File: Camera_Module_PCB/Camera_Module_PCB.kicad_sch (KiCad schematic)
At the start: 58 parts, among them J2 DM3AT-SF-PEJM5, J3 FFC2A32-24-T, J4 Conn_01x02, SW2 SW_Push, SW3 SW_Push, U2 ESP32-S3R8, U4 MAX98357AETE_T, U5 MSM261DGT003, U6 SY7200AABC, Y1 40MHz

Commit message: Minor Changes
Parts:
- renumbered U5 to Mic
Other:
- note added: "ESP 32 and Supporting Schematics"
- note added: "Microphone"
- note added: "Optical Sensor"
- note removed: "Are pull-up resistors needed because I2C communication requires idle high?"
- note removed: "Honestly idk why the resistors are used here. If u know please lmk why."
- note removed: "Made all conections to the MCU, but there is still the issue of power. I cannot find alternative regulators for 2.8 & 1.5. I'm sure I can find some soon tho"
- moved on the sheet: C, C1, C11, C12, C13, C14, C15, C16, C2, C24, C25, C26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

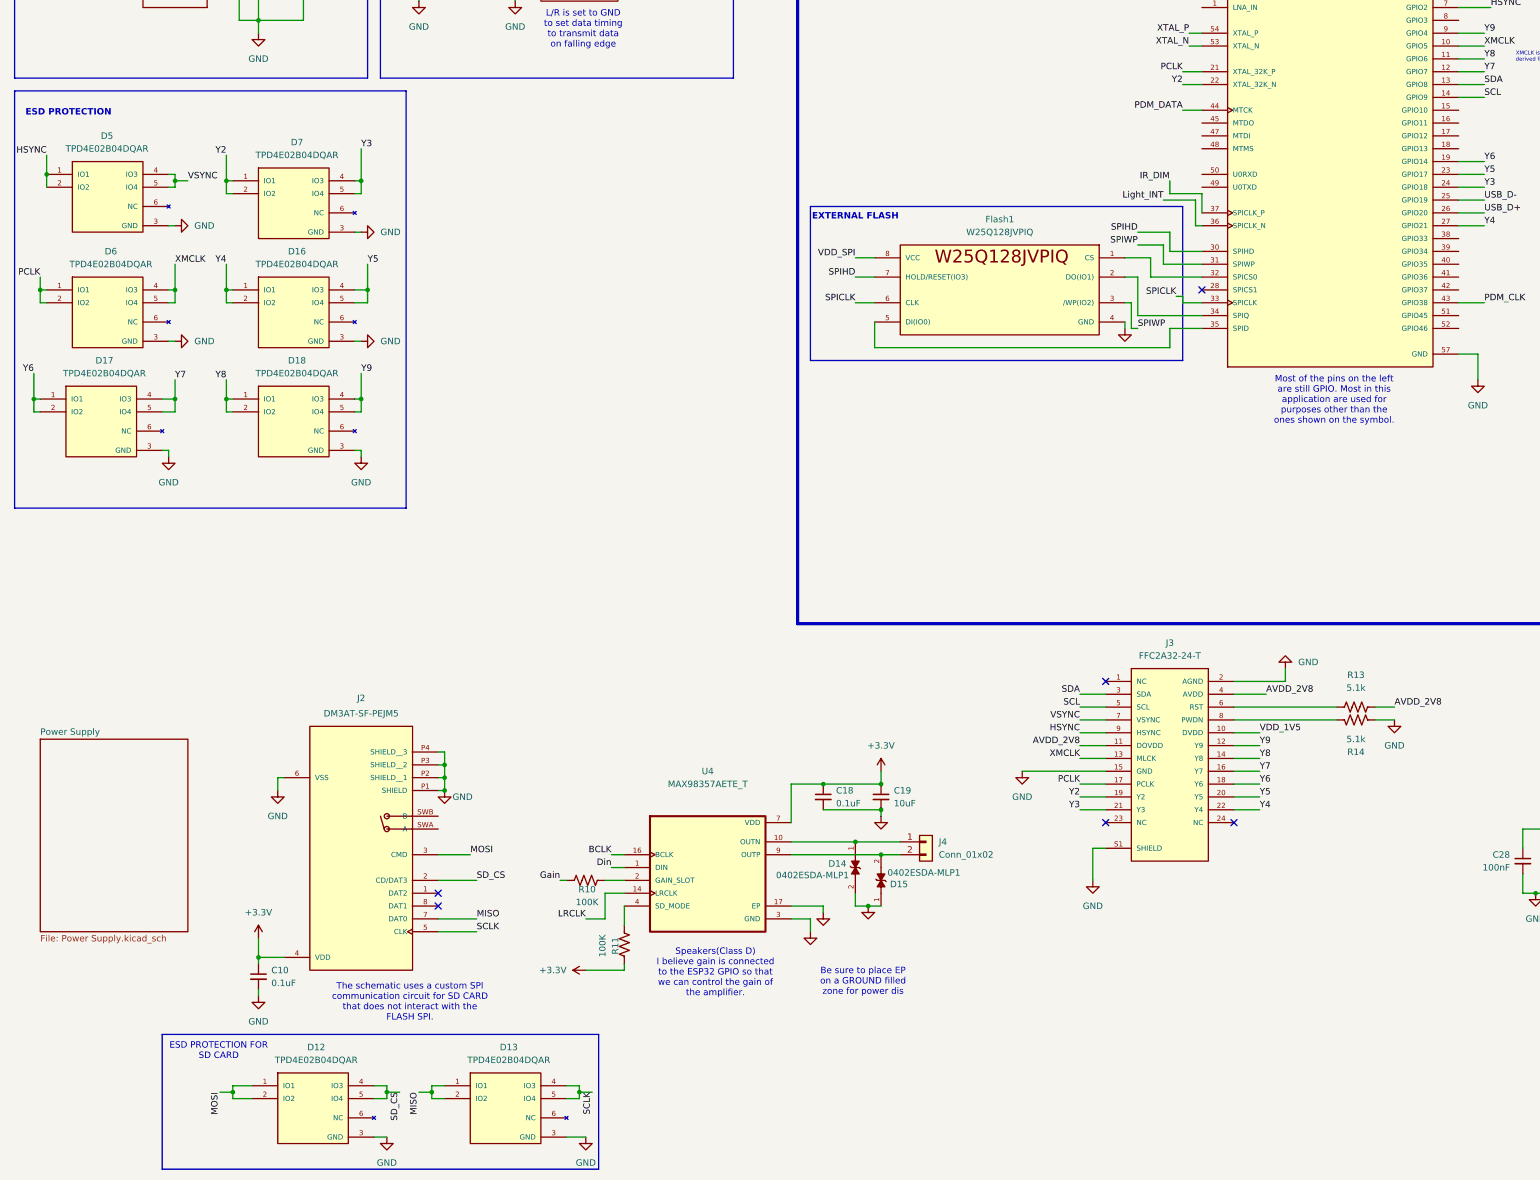
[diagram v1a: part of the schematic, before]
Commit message: V1.1.0
Preliminary Schematic needs a couple of changes left to be made.
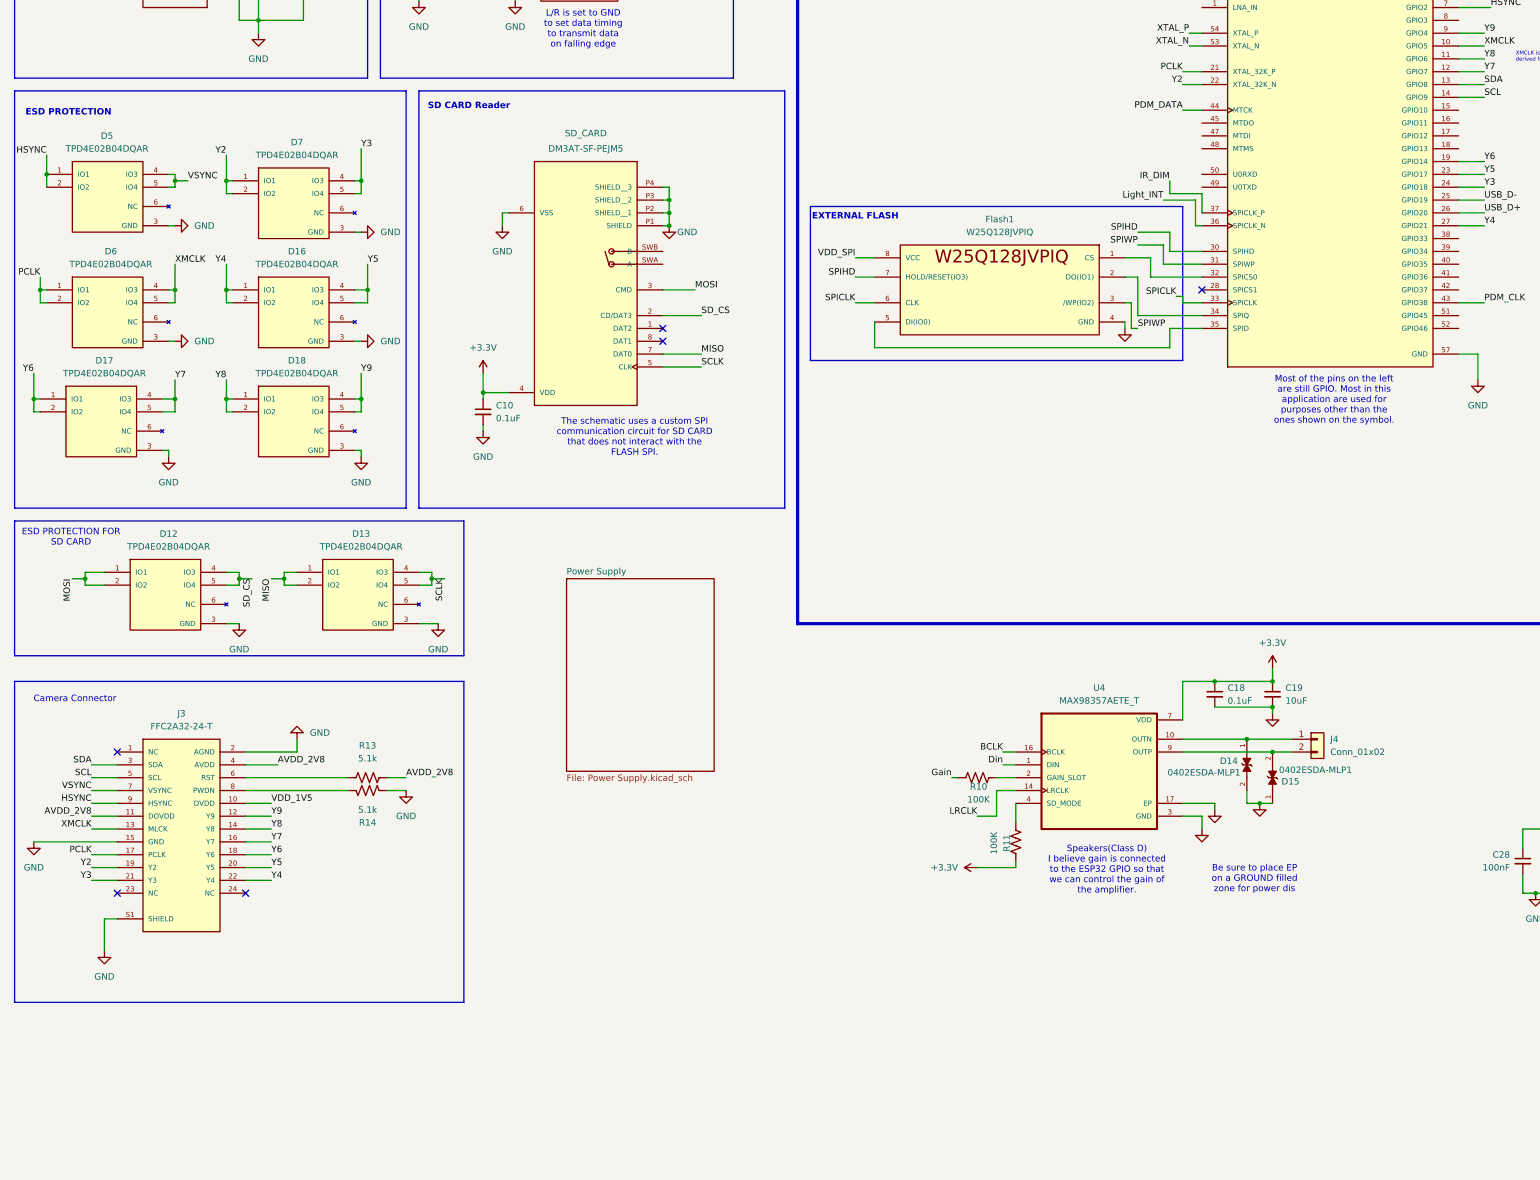
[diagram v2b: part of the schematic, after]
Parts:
- renumbered J2 to SD_CARD
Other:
- note added: "Camera Connector"
- note added: "SD CARD Reader"
- moved on the sheet: C10, C18, C19, D12, D13, D14, D15, J3, J4, R10, R11, R13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

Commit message: N.A
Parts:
- added C30: 0.1uF, symbol Device:C_Small
- added C31: 1uF, symbol Device:C_Small
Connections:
- net +3.3V: now also U2.29 (VDD_SPI), C30.1, C31.1
- net GND: now also C30.2, C31.2
- net VDD_SPI: no longer U2.29 (VDD_SPI)
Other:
- note added: "Basically 1 Decap per VDD pin and 1 Bulk During placment just put the caps next to the pins."
- note added: "Good Work Explaining why L/R is set to ground"
- note added: "Was there a reason why there isnt a pull up on the light_int"
- moved on the sheet: C16, C6

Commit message: Made Minor Changes and Reviewed Schematic
Only a few more connections must be made to the ESP32 component. All other components should be complete.
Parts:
- added R15: 10K, symbol Device:R_US
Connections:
- net +3.3V: now also R15.1
- net BCLK: now also U2.51 (GPIO45)
- net LRCLK: now also U2.52 (GPIO46)
- net Light_INT: now also R15.2
- net MISO: now also U2.18 (GPIO13)
- net MOSI: now also U2.16 (GPIO11)
- net SCLK: no longer SD_CARD.5 (CLK)
- net SD_CS: now also U2.15 (GPIO10)
- net SD_CLK: now reaches U2.17 (GPIO12)
- net SD_CLK: now also SD_CARD.5 (CLK)
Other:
- note added: "ESD PROTECTION - CAMERA MODULE"
- note added: "I made a mistake while wiring. Initially I had a version without INT so when i replaced i forgot to add pull-up"
- note added: "Interrupt needs a pullup since it is an open drain output. When it sends the interrupt signal it will go low. This will be needed for programming"
- note removed: "ESD PROTECTION"
- note removed: "Was there a reason why there isnt a pull up on the light_int"
- moved on the sheet: R1, R2

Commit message: no
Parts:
- removed C26, C28: 100nF, symbol Device:C_Small
- removed C27, C29: 10uF, symbol Device:C_Small
- removed D19: D_Schottky, symbol Device:D_Schottky
- removed L4: L, symbol Device:L
- removed R12: R_US, symbol Device:R_US
- removed U6: SY7200AABC, SY7200AABC:SOT-23-6_L2.9-W1.6-P0.95-LS2.8-BR, symbol SY7200AABC:SY7200AABC
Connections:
- net Din: now also U2.48 (MTMS)
- net Gain: now also U2.47 (MTDI)
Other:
- note added: "Amplifier for Speaker"
- note removed: "All passive elements are not final values. We must determine them using the equations provided in the datasheet."
- note removed: "Basically 1 Decap per VDD pin and 1 Bulk During placment just put the caps next to the pins."
- note removed: "Good Work Explaining why L/R is set to ground"
- note removed: "I made a mistake while wiring. Initially I had a version without INT so when i replaced i forgot to add pull-up"
- note removed: "IR Diode array"
- moved on the sheet: C18, C19, D14, D15, J4, R10, R11, R15, U4

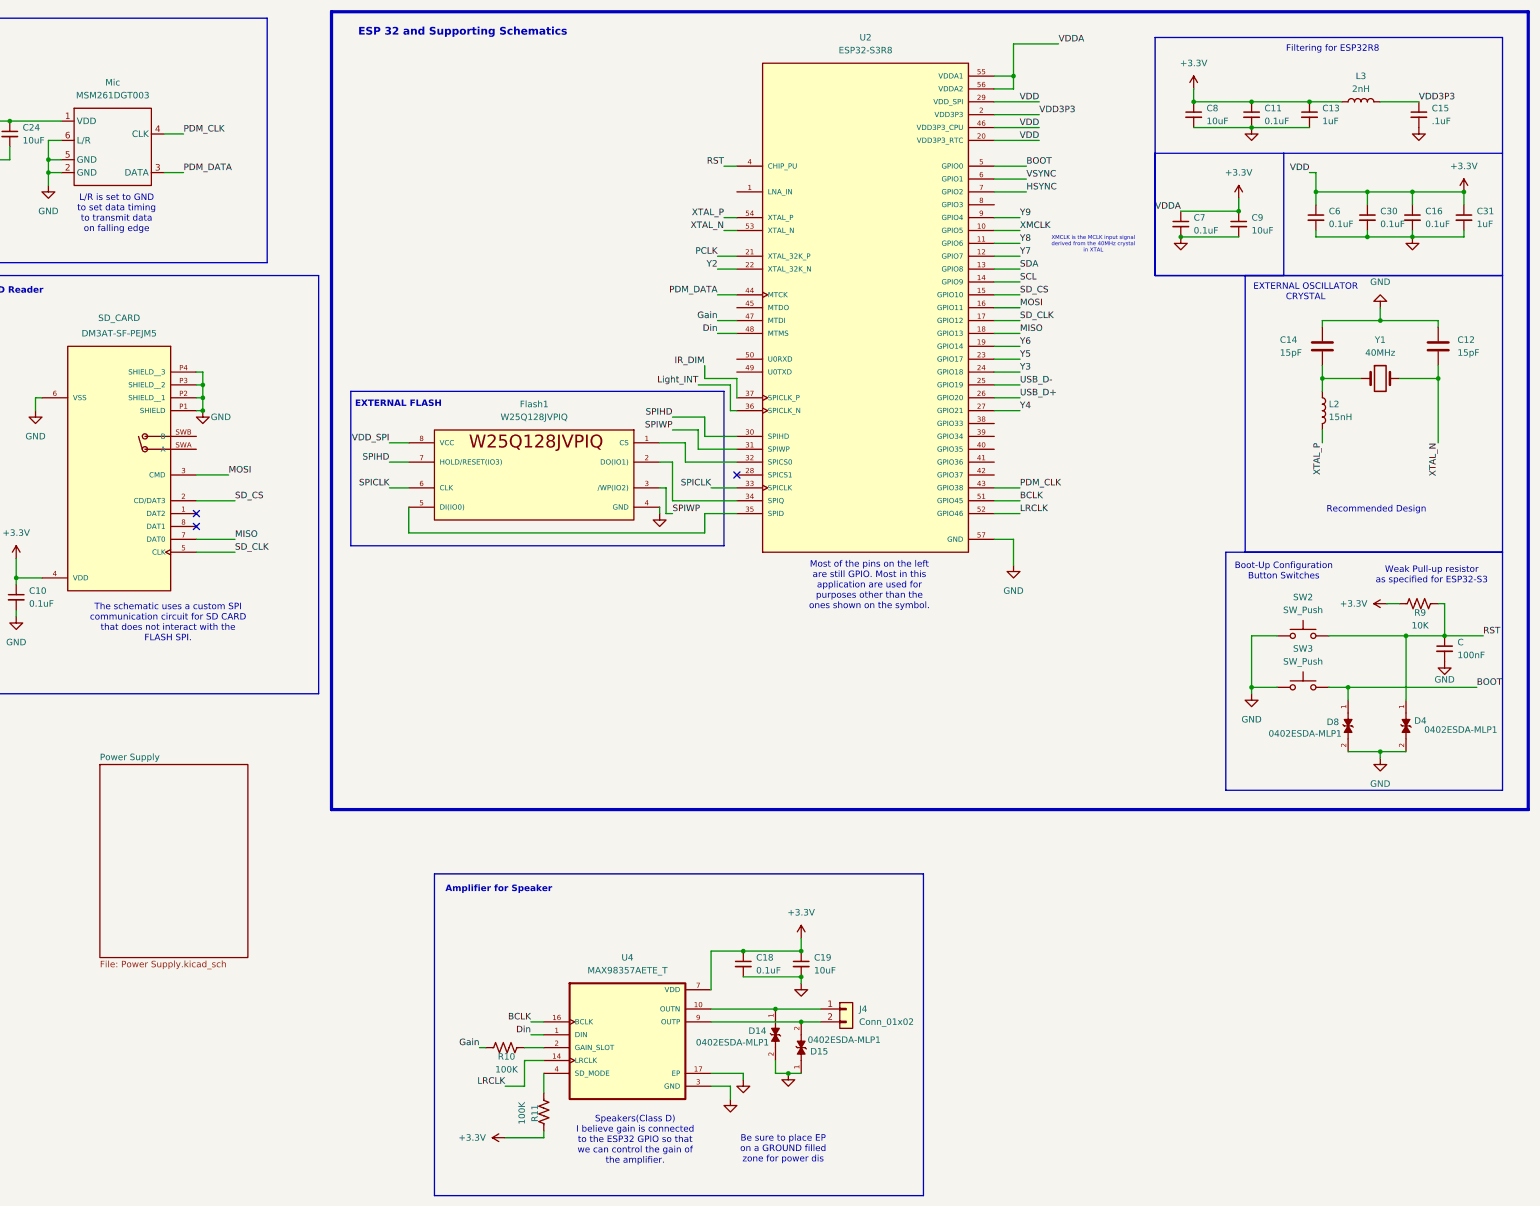
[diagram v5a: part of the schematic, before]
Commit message: Compiled Footprints and Set up PCB layout
All of the footprints that correspond to the schematic symbols were properly referenced in the schematic annotations. The PCB layout was then updated to contain all of the appropriate footprints. Finally, a large ground filled zone was created with dimensions of about 42mm x 42mm as a starting base for the PCB size.
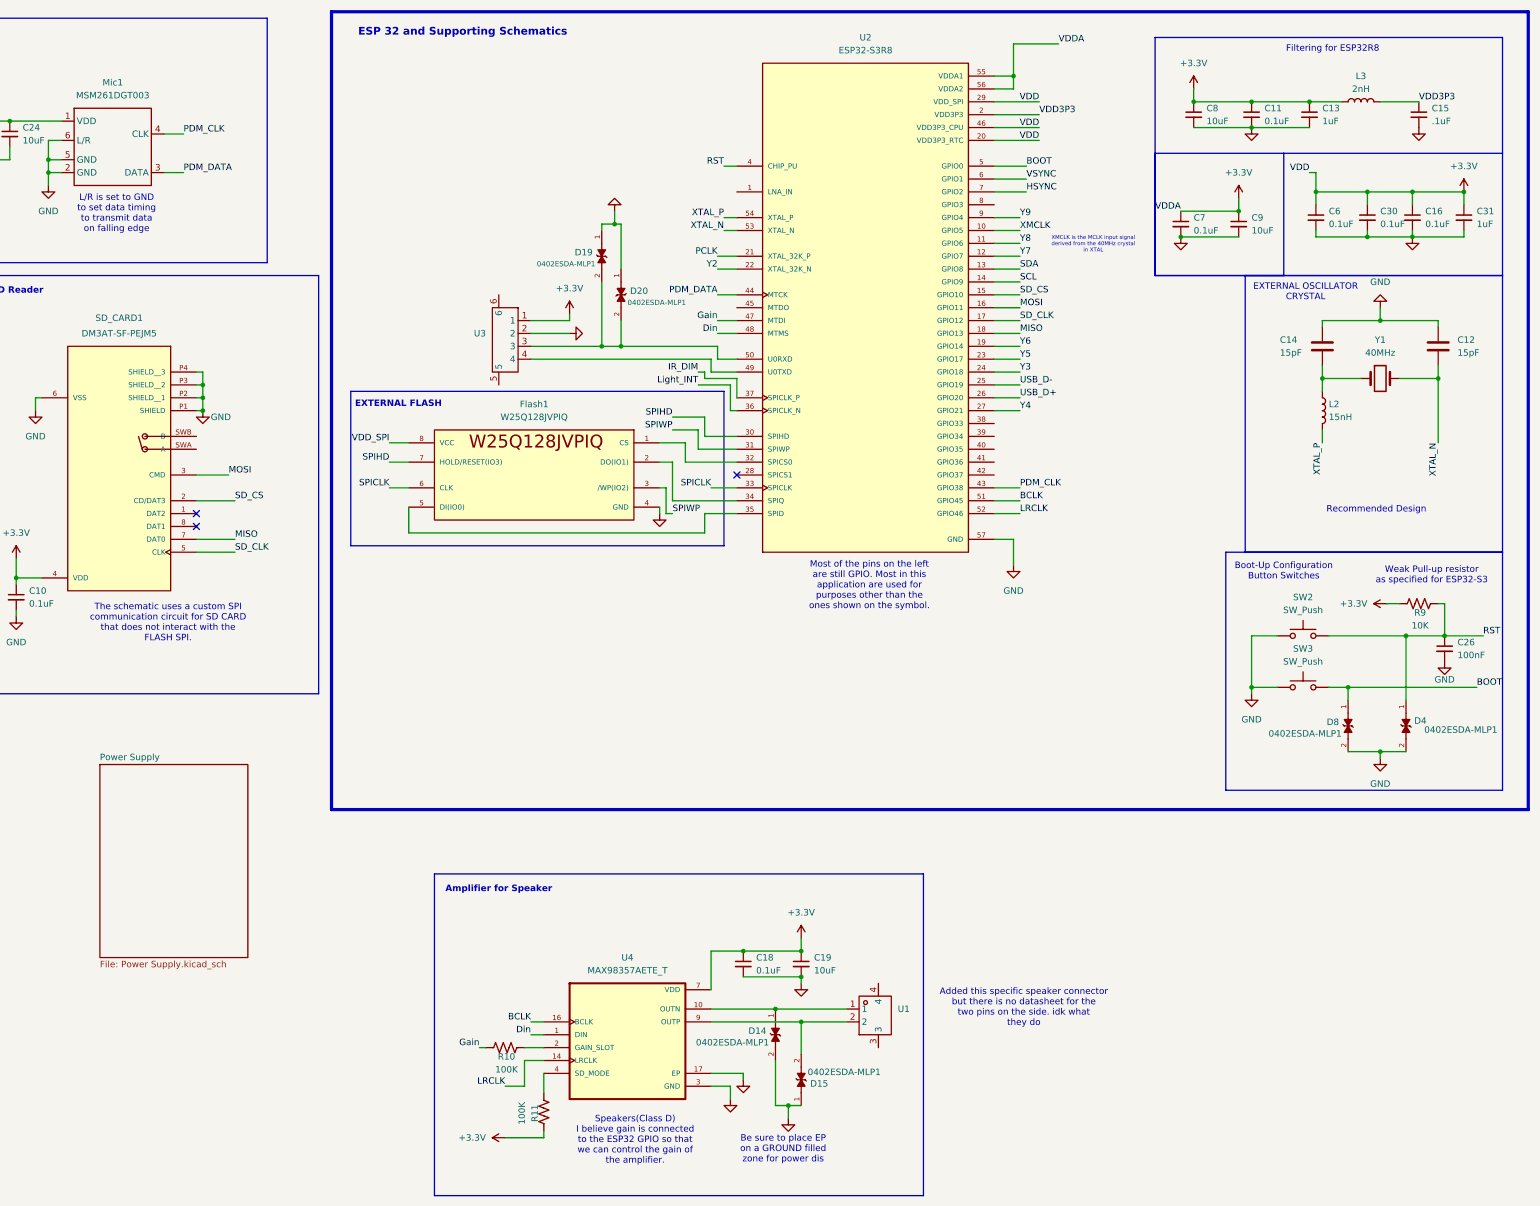
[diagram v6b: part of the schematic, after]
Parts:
- removed J4: Conn_01x02, symbol Connector_Generic:Conn_01x02
- added D19, D20: 0402ESDA-MLP1, ESP32CAM_Foorprints:ESD_0402ESDA-MLP1, symbol 0402ESDA-MLP1:0402ESDA-MLP1
- added U1: ~, XUNPU WAFER-MX1.25-2PWB:CONN-SMD_2P-P1.25_XUNPU_WAFER-MX1.25-2PWB, symbol XUNPU WAFER-MX1.25-2PWB:WAFER-MX1.25-2PWB
- added U3: ~, Bossie BX-PH2.0-4PWT:CONN-SMD_4P-P2.00_BX-PH-2.0-4PWT, symbol Bossie BX-PH2.0-4PWT:BX-PH2.0-4PWT
- C1, C10, C11, C12, C13, C14, C15, C16, C18, C19, C2, C24, C25, C30, C31, C6, C7, C8, C9: footprint (none) -> Capacitor_SMD:C_0603_1608Metric
- C26: renamed from C; footprint (none) -> Capacitor_SMD:C_0603_1608Metric
- D12, D13, D16, D17, D18, D5, D6, D7: footprint TPD4E02B04DQAR:DIO_TPD4E02B04DQAR -> ESP32CAM_Foorprints:DIO_TPD4E02B04DQAR
- D14, D15, D4, D8: footprint 0402ESDA-MLP1:ESD_0402ESDA-MLP1 -> ESP32CAM_Foorprints:ESD_0402ESDA-MLP1
- Flash1: footprint W25Q128JVPIQ:W25Q128JVPIQ -> ESP32CAM_Foorprints:W25Q128JVPIQ
- J3: footprint FFC2A32-24-T:GCT_FFC2A32-24-T -> ESP32CAM_Foorprints:GCT_FFC2A32-24-T
- L2, L3: footprint (none) -> Inductor_SMD:L_0603_1608Metric
- R1, R10, R11, R13, R14, R15, R2, R9: footprint (none) -> Resistor_SMD:R_0603_1608Metric
- SD_CARD1: renamed from SD_CARD; footprint DM3AT-SF-PEJM5:HRS_DM3AT-SF-PEJM5 -> ESP32CAM_Foorprints:HRS_DM3AT-SF-PEJM5
- SW2, SW3: footprint (none) -> Button_Switch_SMD:SW_Push_1P1T_NO_CK_KMR2
- U2: footprint ESP32-S3R8:QFN40P700X700X90-57N -> ESP32CAM_Foorprints:QFN40P700X700X90-57N
- U4: footprint MAX98357AETE_T:QFN50P300X300X80-17N -> ESP32CAM_Foorprints:QFN50P300X300X80-17N
- Y1: footprint (none) -> Crystal:Crystal_AT310_D3.0mm_L10.0mm_Horizontal
- renumbered Mic to Mic1
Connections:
- net +3.3V: now also U3.1
- net GND: now also D19.1, D20.1, U3.2
- net at D14.1, U4.10 (OUTN): now also U1.1
- net at D15.2, U4.9 (OUTP): now also U1.2
- net at U2.49 (U0TXD): now also U3.4
- net at U2.50 (U0RXD): now also D19.2, D20.2, U3.3
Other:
- note added: "Added this specific speaker connector but there is no datasheet for the two pins on the side. idk what they do"
- moved on the sheet: D15
